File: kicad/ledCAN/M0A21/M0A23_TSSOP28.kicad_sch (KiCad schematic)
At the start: 4 parts

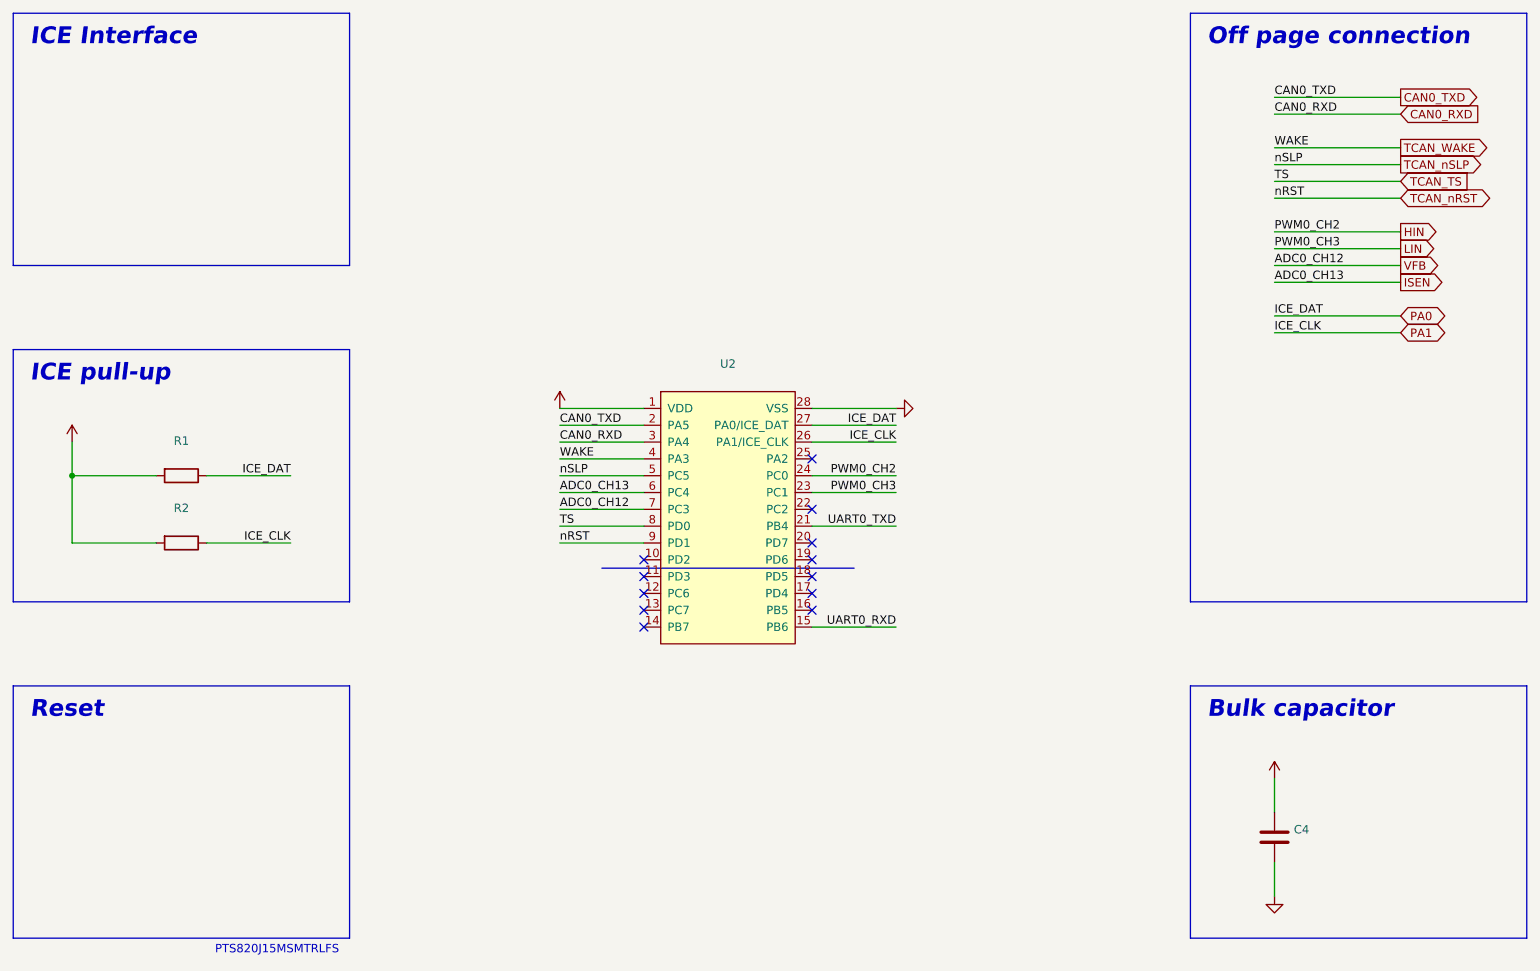
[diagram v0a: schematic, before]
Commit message: Update page settings
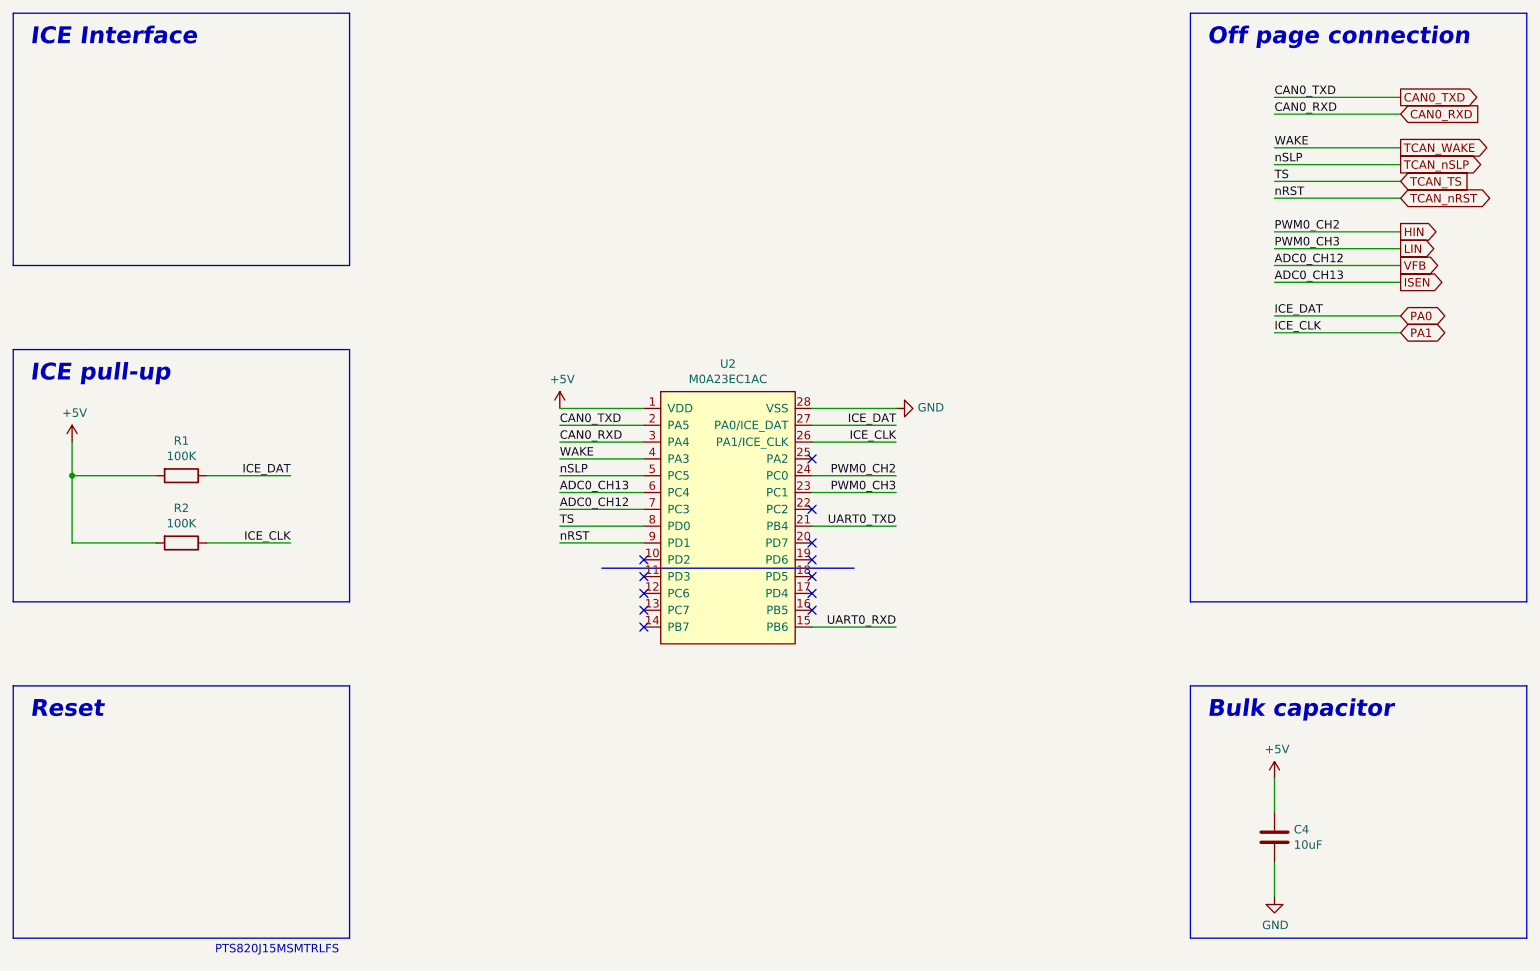
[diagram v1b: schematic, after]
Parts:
- C4: value (none) -> 10uF; footprint (none) -> Capacitor_SMD:C_0805_2012Metric
- R1, R2: value (none) -> 100K; footprint (none) -> Resistor_SMD:R_0603_1608Metric
- U2: value (none) -> M0A23EC1AC; footprint (none) -> Package_SO:TSSOP-28_4.4x9.7mm_P0.65mm
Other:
- company: DANCHOUZHOU -> City Science Lab @ Taipei Tech /a cooperation with the MIT Media Lab
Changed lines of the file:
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@@
   (title_block
     (title "Multi purpose power converter module with CAN bus interface")
-    (date "2021-08-31")
-    (rev "1.1")
-    (company "DANCHOUZHOU")
-    (comment 1 "City Science - MIT Media Lab")
-    (comment 2 "danchouzhou@gmail.com")
+    (date "2022-09-07")
+    (rev "0.1")
+    (company "City Science Lab @ Taipei Tech /a cooperation with the MIT Media Lab")
+    (comment 1 "DANCHOUZHOU")
+    (comment 2 "https://github.com/danchouzhou")
+    (comment 3 "danchouzhou@gmail.com")
   )
   (junction (at 46.99 95.25) (diameter 0) (color 0 0 0 0)
@@
     (in_bom yes) (on_board yes)
     (property "Reference" "U2" (id 0) (at 146.05 78.359 0))
-    (property "Value" "" (id 1) (at 146.05 80.6704 0))
-    (property "Footprint" "" (id 2) (at 146.05 62.23 0)
+    (property "Value" "M0A23EC1AC" (id 1) (at 146.05 80.6704 0))
+    (property "Footprint" "Package_SO:TSSOP-28_4.4x9.7mm_P0.65mm" (id 2) (at 146.05 62.23 0)
       (effects (font (size 1.27 1.27)) hide)
     )
@@
       (effects (font (size 1.27 1.27)) hide)
     )
-    (property "Value" "" (id 1) (at 174.7012 84.963 90)
+    (property "Value" "GND" (id 1) (at 174.7012 84.963 90)
       (effects (font (size 1.27 1.27)) (justify right))
     )
@@
       (effects (font (size 1.27 1.27)) hide)
     )
-    (property "Value" "" (id 1) (at 121.031 80.6958 0))
+    (property "Value" "+5V" (id 1) (at 121.031 80.6958 0))
     (property "Footprint" "" (id 2) (at 120.65 85.09 0)
       (effects (font (size 1.27 1.27)) hide)
@@
       (effects (font (size 1.27 1.27)) (justify left))
     )
-    (property "Value" "" (id 1) (at 231.521 151.003 0)
+    (property "Value" "10uF" (id 1) (at 231.521 151.003 0)
       (effects (font (size 1.27 1.27)) (justify left))
     )
-    (property "Footprint" "" (id 2) (at 229.5652 153.67 0)
+    (property "Footprint" "Capacitor_SMD:C_0805_2012Metric" (id 2) (at 229.5652 153.67 0)
       (effects (font (size 1.27 1.27)) hide)
     )
@@
       (effects (font (size 1.27 1.27)) hide)
     )
-    (property "Value" "" (id 1) (at 228.981 136.5758 0))
+    (property "Value" "+5V" (id 1) (at 228.981 136.5758 0))
     (property "Footprint" "" (id 2) (at 228.6 140.97 0)
       (effects (font (size 1.27 1.27)) hide)
@@
       (effects (font (size 1.27 1.27)) hide)
     )
-    (property "Value" "" (id 1) (at 228.727 163.1442 0))
+    (property "Value" "GND" (id 1) (at 228.727 163.1442 0))
     (property "Footprint" "" (id 2) (at 228.6 158.75 0)
       (effects (font (size 1.27 1.27)) hide)
@@
     (in_bom yes) (on_board yes)
     (property "Reference" "R1" (id 0) (at 63.5 89.9922 90))
-    (property "Value" "" (id 1) (at 63.5 92.3036 90))
-    (property "Footprint" "" (id 2) (at 63.5 93.472 90)
+    (property "Value" "100K" (id 1) (at 63.5 92.3036 90))
+    (property "Footprint" "Resistor_SMD:R_0603_1608Metric" (id 2) (at 63.5 93.472 90)
       (effects (font (size 1.27 1.27)) hide)
     )
@@
     (in_bom yes) (on_board yes)
     (property "Reference" "R2" (id 0) (at 63.5 100.1522 90))
-    (property "Value" "" (id 1) (at 63.5 102.4636 90))
-    (property "Footprint" "" (id 2) (at 63.5 103.632 90)
+    (property "Value" "100K" (id 1) (at 63.5 102.4636 90))
+    (property "Footprint" "Resistor_SMD:R_0603_1608Metric" (id 2) (at 63.5 103.632 90)
       (effects (font (size 1.27 1.27)) hide)
     )
@@
       (effects (font (size 1.27 1.27)) hide)
     )
-    (property "Value" "" (id 1) (at 47.371 85.7758 0))
+    (property "Value" "+5V" (id 1) (at 47.371 85.7758 0))
     (property "Footprint" "" (id 2) (at 46.99 90.17 0)
       (effects (font (size 1.27 1.27)) hide)
